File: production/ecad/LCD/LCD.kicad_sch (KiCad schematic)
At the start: 1 part, among them J2 214721-0100

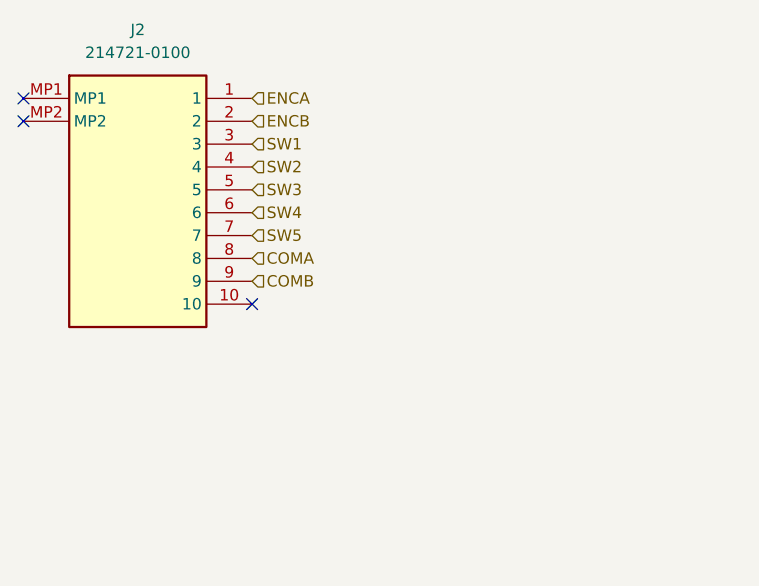
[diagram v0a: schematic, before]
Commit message: added motor/LCD
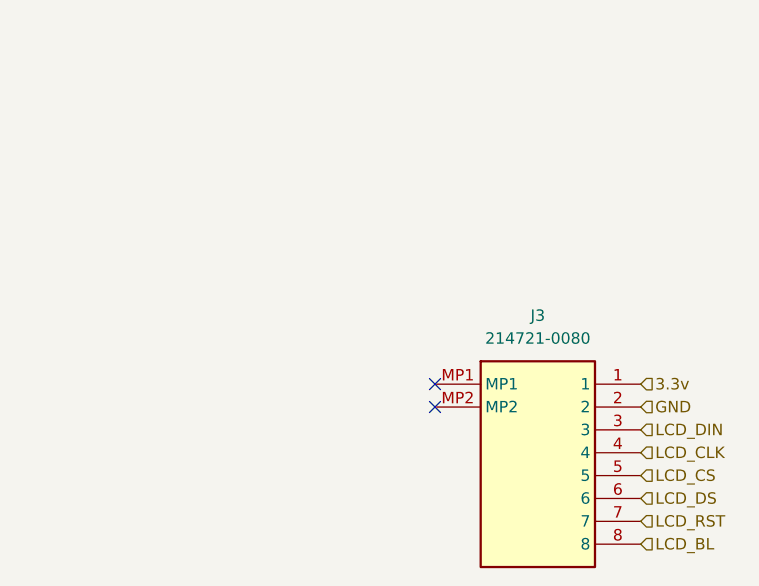
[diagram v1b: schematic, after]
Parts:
- removed J2: 214721-0100, 2147210100, symbol dialheader:214721-0100
- added J3: 214721-0080, 2147210080, symbol 8positionheader:214721-0080
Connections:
- new net 3.3v: J3.1
- new net GND: J3.2
- new net LCD_BL: J3.8
- new net LCD_CLK: J3.4
- new net LCD_CS: J3.5
- new net LCD_DIN: J3.3
- new net LCD_DS: J3.6
- new net LCD_RST: J3.7
- no-connect marks 3 -> 2
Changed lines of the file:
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@@
 	(paper "A4")
 	(no_connect
-		(at 119.38 91.44)
+		(at 139.7 102.87)
 	)
 	(no_connect
-		(at 93.98 68.58)
-	)
-	(no_connect
-		(at 93.98 71.12)
-	)
-	(hierarchical_label "SW1"
-		(shape input)
-		(at 119.38 73.66 0)
-		(fields_autoplaced yes)
-		(effects
-			(font
-				(size 1.27 1.27)
-			)
-			(justify left)
-		)
-	)
-	(hierarchical_label "COMB"
-		(shape input)
-		(at 119.38 88.9 0)
-		(fields_autoplaced yes)
-		(effects
-			(font
-				(size 1.27 1.27)
-			)
-			(justify left)
-		)
-	)
-	(hierarchical_label "ENCA"
-		(shape input)
-		(at 119.38 68.58 0)
-		(fields_autoplaced yes)
-		(effects
-			(font
-				(size 1.27 1.27)
-			)
-			(justify left)
-		)
-	)
-	(hierarchical_label "SW3"
-		(shape input)
-		(at 119.38 78.74 0)
-		(fields_autoplaced yes)
-		(effects
-			(font
-				(size 1.27 1.27)
-			)
-			(justify left)
-		)
-	)
-	(hierarchical_label "ENCB"
-		(shape input)
-		(at 119.38 71.12 0)
-		(fields_autoplaced yes)
-		(effects
-			(font
-				(size 1.27 1.27)
-			)
-			(justify left)
-		)
-	)
-	(hierarchical_label "SW2"
-		(shape input)
-		(at 119.38 76.2 0)
-		(fields_autoplaced yes)
-		(effects
-			(font
-				(size 1.27 1.27)
-			)
-			(justify left)
-		)
-	)
-	(hierarchical_label "SW5"
-		(shape input)
-		(at 119.38 83.82 0)
-		(fields_autoplaced yes)
-		(effects
-			(font
-				(size 1.27 1.27)
-			)
-			(justify left)
-		)
-	)
-	(hierarchical_label "COMA"
-		(shape input)
-		(at 119.38 86.36 0)
-		(fields_autoplaced yes)
-		(effects
-			(font
-				(size 1.27 1.27)
-			)
-			(justify left)
-		)
-	)
-	(hierarchical_label "SW4"
-		(shape input)
-		(at 119.38 81.28 0)
+		(at 139.7 100.33)
+	)
+	(hierarchical_label "LCD_CLK"
+		(shape input)
+		(at 162.56 107.95 0)
+		(fields_autoplaced yes)
+		(effects
+			(font
+				(size 1.27 1.27)
+			)
+			(justify left)
+		)
+	)
+	(hierarchical_label "LCD_DIN"
+		(shape input)
+		(at 162.56 105.41 0)
+		(fields_autoplaced yes)
+		(effects
+			(font
+				(size 1.27 1.27)
+			)
+			(justify left)
+		)
+	)
+	(hierarchical_label "LCD_RST"
+		(shape input)
+		(at 162.56 115.57 0)
+		(fields_autoplaced yes)
+		(effects
+			(font
+				(size 1.27 1.27)
+			)
+			(justify left)
+		)
+	)
+	(hierarchical_label "3.3v"
+		(shape input)
+		(at 162.56 100.33 0)
+		(fields_autoplaced yes)
+		(effects
+			(font
+				(size 1.27 1.27)
+			)
+			(justify left)
+		)
+	)
+	(hierarchical_label "LCD_CS"
+		(shape input)
+		(at 162.56 110.49 0)
+		(fields_autoplaced yes)
+		(effects
+			(font
+				(size 1.27 1.27)
+			)
+			(justify left)
+		)
+	)
+	(hierarchical_label "LCD_DS"
+		(shape input)
+		(at 162.56 113.03 0)
+		(fields_autoplaced yes)
+		(effects
+			(font
+				(size 1.27 1.27)
+			)
+			(justify left)
+		)
+	)
+	(hierarchical_label "GND"
+		(shape input)
+		(at 162.56 102.87 0)
+		(fields_autoplaced yes)
+		(effects
+			(font
+				(size 1.27 1.27)
+			)
+			(justify left)
+		)
+	)
+	(hierarchical_label "LCD_BL"
+		(shape input)
+		(at 162.56 118.11 0)
 		(fields_autoplaced yes)
 		(effects
@@
 	)
 	(symbol
-		(lib_id "dialheader:214721-0100")
-		(at 93.98 68.58 0)
+		(lib_id "8positionheader:214721-0080")
+		(at 139.7 100.33 0)
 		(unit 1)
 		(exclude_from_sim no)
@@
 		(dnp no)
 		(fields_autoplaced yes)
-		(property "Reference" "J2"
-			(at 106.68 60.96 0)
-			(effects
-				(font
-					(size 1.27 1.27)
-				)
-			)
-		)
-		(property "Value" "214721-0100"
-			(at 106.68 63.5 0)
-			(effects
-				(font
-					(size 1.27 1.27)
-				)
-			)
-		)
-		(property "Footprint" "2147210100"
-			(at 115.57 163.5 0)
-			(effects
-				(font
-					(size 1.27 1.27)
-				)
-				(justify left top)
-				(hide yes)
-			)
-		)
-		(property "Datasheet" "https://www.molex.com/pdm_docs/sd/2147210100_sd.pdf"
-			(at 115.57 263.5 0)
-			(effects
-				(font
-					(size 1.27 1.27)
-				)
-				(justify left top)
-				(hide yes)
-			)
-		)
-		(property "Description" "MOLEX - 214721-0100 - Pin Header, Signal, Wire-to-Board, 0.8 mm, 1 Rows, 10 Contacts, Surface Mount Right Angle"
-			(at 93.98 68.58 0)
+		(property "Reference" "J3"
+			(at 151.13 92.71 0)
+			(effects
+				(font
+					(size 1.27 1.27)
+				)
+			)
+		)
+		(property "Value" "214721-0080"
+			(at 151.13 95.25 0)
+			(effects
+				(font
+					(size 1.27 1.27)
+				)
+			)
+		)
+		(property "Footprint" "2147210080"
+			(at 158.75 195.25 0)
+			(effects
+				(font
+					(size 1.27 1.27)
+				)
+				(justify left top)
+				(hide yes)
+			)
+		)
+		(property "Datasheet" "https://www.molex.com/pdm_docs/sd/2147210080_sd.pdf"
+			(at 158.75 295.25 0)
+			(effects
+				(font
+					(size 1.27 1.27)
+				)
+				(justify left top)
+				(hide yes)
+			)
+		)
+		(property "Description" "Zero-Hachi Header, 0.80mm Pitch, Single Row, Right-Angle, Surface Mount, Matte Tin (Sn) Plating, Friction Lock, 8 Circuits, Tape and Reel"
+			(at 139.7 100.33 0)
 			(effects
 				(font
@@
 		)
 		(property "Height" "1.8"
-			(at 115.57 463.5 0)
-			(effects
-				(font
-					(size 1.27 1.27)
-				)
-				(justify left top)
-				(hide yes)
-			)
-		)
-		(property "Mouser Part Number" "538-214721-0100"
-			(at 115.57 563.5 0)
-			(effects
-				(font
-					(size 1.27 1.27)
-				)
-				(justify left top)
-				(hide yes)
-			)
-		)
-		(property "Mouser Price/Stock" "https://www.mouser.co.uk/ProductDetail/Molex/214721-0100?qs=MyNHzdoqoQJCc4Zxlj0GUQ%3D%3D"
-			(at 115.57 663.5 0)
+			(at 158.75 495.25 0)
+			(effects
+				(font
+					(size 1.27 1.27)
+				)
+				(justify left top)
+				(hide yes)
+			)
+		)
+		(property "Mouser Part Number" ""
+			(at 158.75 595.25 0)
+			(effects
+				(font
+					(size 1.27 1.27)
+				)
+				(justify left top)
+				(hide yes)
+			)
+		)
+		(property "Mouser Price/Stock" ""
+			(at 158.75 695.25 0)
 			(effects
 				(font
@@
 		)
 		(property "Manufacturer_Name" "Molex"
-			(at 115.57 763.5 0)
-			(effects
-				(font
-					(size 1.27 1.27)
-				)
-				(justify left top)
-				(hide yes)
-			)
-		)
-		(property "Manufacturer_Part_Number" "214721-0100"
-			(at 115.57 863.5 0)
-			(effects
-				(font
-					(size 1.27 1.27)
-				)
-				(justify left top)
-				(hide yes)
-			)
-		)
-		(pin "10"
+			(at 158.75 795.25 0)
+			(effects
+				(font
+					(size 1.27 1.27)
+				)
+				(justify left top)
+				(hide yes)
+			)
+		)
+		(property "Manufacturer_Part_Number" "214721-0080"
+			(at 158.75 895.25 0)
+			(effects
+				(font
+					(size 1.27 1.27)
+				)
+				(justify left top)
+				(hide yes)
+			)
+		)
+		(pin "7"
+		)
+		(pin "2"
+		)
+		(pin "MP1"
+		)
+		(pin "6"
 		)
 		(pin "3"
 		)
+		(pin "MP2"
+		)
+		(pin "8"
+		)
+		(pin "5"
+		)
+		(pin "1"
+		)
 		(pin "4"
 		)
-		(pin "MP2"
-		)
-		(pin "5"
-		)
-		(pin "2"
-		)
-		(pin "6"
-		)
-		(pin "8"
-		)
-		(pin "9"
-		)
-		(pin "MP1"
-		)
-		(pin "1"
-		)
-		(pin "7"
-		)
 		(instances
-			(project ""
-				(path "/a34d77bc-8f6a-417e-a206-3165e6c5c658/56db885d-6988-4ba3-9c6c-3dd30ffbc985"
-					(reference "J2")
+			(project "Main"
+				(path "/a34d77bc-8f6a-417e-a206-3165e6c5c658/6d945d10-bd0c-4453-b6e0-f783497d7a3f"
+					(reference "J3")
 					(unit 1)
 				)

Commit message: connectors
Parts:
- J3: footprint 2147210080 -> Footprints:8positionheader
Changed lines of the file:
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@@
 			)
 		)
-		(property "Footprint" "2147210080"
+		(property "Footprint" "Footprints:8positionheader"
 			(at 158.75 195.25 0)
 			(effects

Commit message: schematic changes and pcb
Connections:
- net GND: now also J3.MP1, J3.MP2
- no-connect marks 2 -> 0
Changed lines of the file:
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@@
 	(generator_version "8.0")
 	(paper "A4")
-	(no_connect
-		(at 139.7 102.87)
-	)
-	(no_connect
-		(at 139.7 100.33)
-	)
 	(hierarchical_label "LCD_CLK"
 		(shape input)
@@
 					(unit 1)
 				)
+			)
+		)
+	)
+	(symbol
+		(lib_id "power:GND")
+		(at 139.7 102.87 270)
+		(unit 1)
+		(exclude_from_sim no)
+		(in_bom yes)
+		(on_board yes)
+		(dnp no)
+		(property "Reference" "#PWR057"
+			(at 133.35 102.87 0)
+			(effects
+				(font
+					(size 1.27 1.27)
+				)
+				(hide yes)
+			)
+		)
+		(property "Value" "GND"
+			(at 135.89 102.8701 90)
+			(effects
+				(font
+					(size 1.27 1.27)
+				)
+				(justify right)
+			)
+		)
+		(property "Footprint" ""
+			(at 139.7 102.87 0)
+			(effects
+				(font
+					(size 1.27 1.27)
+				)
+				(hide yes)
+			)
+		)
+		(property "Datasheet" ""
+			(at 139.7 102.87 0)
+			(effects
+				(font
+					(size 1.27 1.27)
+				)
+				(hide yes)
+			)
+		)
+		(property "Description" "Power symbol creates a global label with name \"GND\" , ground"
+			(at 139.7 102.87 0)
+			(effects
+				(font
+					(size 1.27 1.27)
+				)
+				(hide yes)
+			)
+		)
+		(pin "1"
+		)
+		(instances
+			(project "Main"
+				(path "/a34d77bc-8f6a-417e-a206-3165e6c5c658/6d945d10-bd0c-4453-b6e0-f783497d7a3f"
+					(reference "#PWR057")
+					(unit 1)
+				)
+			)
+		)
+	)
+	(symbol
+		(lib_id "power:GND")
+		(at 139.7 100.33 270)
+		(unit 1)
+		(exclude_from_sim no)
+		(in_bom yes)
+		(on_board yes)
+		(dnp no)
+		(property "Reference" "#PWR056"
+			(at 133.35 100.33 0)
+			(effects
+				(font
+					(size 1.27 1.27)
+				)
+				(hide yes)
+			)
+		)
+		(property "Value" "GND"
+			(at 135.89 100.3301 90)
+			(effects
+				(font
+					(size 1.27 1.27)
+				)
+				(justify right)
+			)
+		)
+		(property "Footprint" ""
+			(at 139.7 100.33 0)
+			(effects
+				(font
+					(size 1.27 1.27)
+				)
+				(hide yes)
+			)
+		)
+		(property "Datasheet" ""
+			(at 139.7 100.33 0)
+			(effects
+				(font
+					(size 1.27 1.27)
+				)
+				(hide yes)
+			)
+		)
+		(property "Description" "Power symbol creates a global label with name \"GND\" , ground"
+			(at 139.7 100.33 0)
+			(effects
+				(font
+					(size 1.27 1.27)
+				)
+				(hide yes)
+			)
+		)
+		(pin "1"
+		)
+		(instances
+			(project "Main"
+				(path "/a34d77bc-8f6a-417e-a206-3165e6c5c658/6d945d10-bd0c-4453-b6e0-f783497d7a3f"
+					(reference "#PWR056")
+					(unit 1)
+				)
